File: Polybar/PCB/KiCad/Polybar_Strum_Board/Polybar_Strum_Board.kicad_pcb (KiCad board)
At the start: 2 copper layers, 185 x 38 mm, 25 parts, among them SW1 MX_SW_solder, SW2 MX_SW_solder, SW3 MX_SW_solder, SW4 MX_SW_HS, SW5 MX_SW_HS, U1 ProMicro, U2 RKJXV1224005

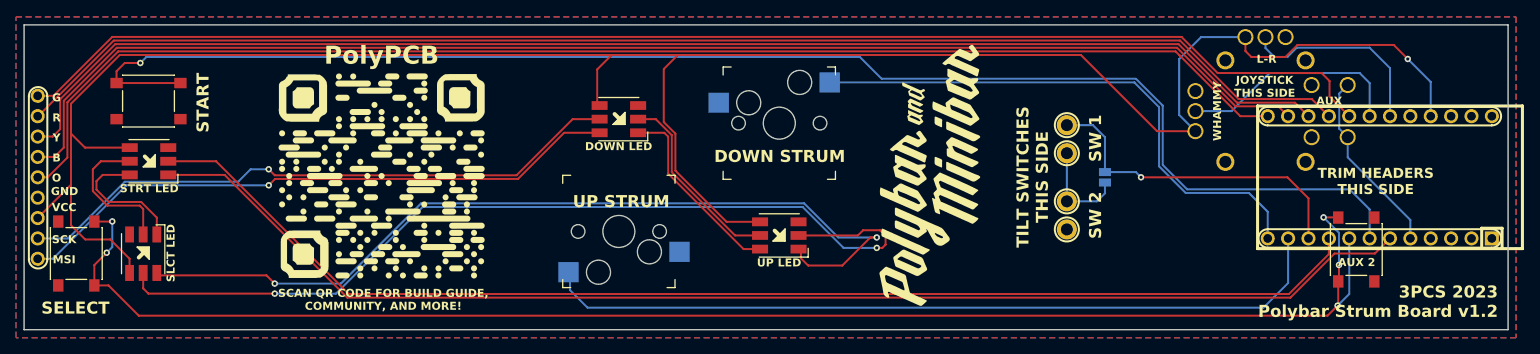
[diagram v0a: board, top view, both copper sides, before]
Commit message: Switched connectors from test pins to an actual connector
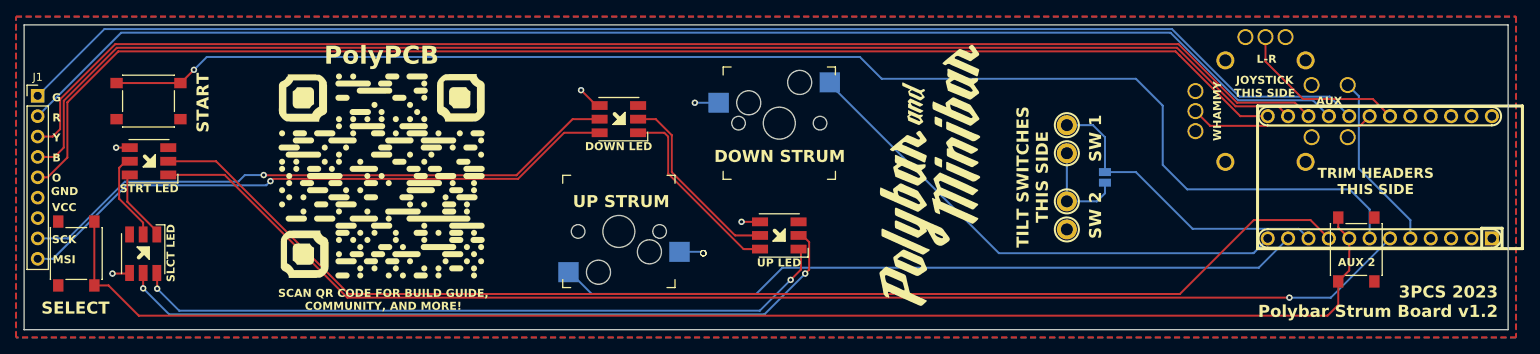
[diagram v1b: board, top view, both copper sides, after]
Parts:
- removed TP10, TP11, TP12, TP14, TP15, TP16, TP4, TP6, TP8: TestPoint, Polybar:test_point
- added J1: Conn_01x09_Pin, Connector_PinHeader_2.54mm:PinHeader_1x09_P2.54mm_Vertical, F.Cu at (23.7, 104.8)
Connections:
- SW1 pad 1: Select -> GND
- SW1 pad 2: GND -> Select
- SW3 pad 1: GND -> Start
- SW3 pad 2: Start -> GND
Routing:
- net VCC: track 273.4 -> 9.26 mm, vias 1 -> 4
- net 2_mosi: track 108.5 -> 87.7 mm
- net 2_sck: track 113.4 -> 93.1 mm
- net Select: track 190.9 -> 177.2 mm, vias 5 -> 0
- net Start: track 182.2 -> 173.4 mm
- net 3_mosi: track 16.0 -> 8.65 mm
- net 3_sck: track 17.5 -> 10.6 mm
- net GND: track 0.00 -> 6.01 mm, vias 0 -> 5
- net Up: track 99.5 -> 93.5 mm
- net VRY: track 28.3 -> 23.0 mm
- net Down: track 69.1 -> 64.4 mm
- net VRX: track 24.9 -> 21.4 mm
- net Tilt: track 41.4 -> 38.5 mm, vias 1 -> 0
- net SW: track 23.2 -> 22.4 mm
- net Red: track 168.8 -> 169.6 mm
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- added copper zone on B.Cu, net VCC
- added copper zone on F.Cu, net VCC
- removed copper zone on B.Cu, net GND

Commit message: re-routed pcb
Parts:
- removed TP1, TP17, TP2, TP3: TestPoint, Polybar:test_point_2
- added SJ2: Conn_01x02_Pin, Connector_PinHeader_2.54mm:PinHeader_1x02_P2.54mm_Vertical, F.Cu at (152.0, 119.4)
- added SJ3: Conn_01x02_Pin, Connector_PinHeader_2.54mm:PinHeader_1x02_P2.54mm_Vertical, F.Cu at (152.0, 109.2)
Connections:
- D1 pad 5: fret_sck -> 2_sck
- D1 pad 6: fret_mosi -> 2_mosi
- D2 pad 1: 2_mosi -> led_mosi
- D2 pad 2: 2_sck -> led_sck
- D3 pad 5: 2_sck -> fret_mosi
- D3 pad 6: 2_mosi -> fret_sck
- D4 pad 1: led_mosi -> 2_mosi
- D4 pad 2: led_sck -> 2_sck
- U2 pad SH: (no net) -> unconnected-(U2-PadSH)
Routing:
- net led_sck: track 156.0 -> 67.3 mm
- net led_mosi: track 161.4 -> 76.8 mm
- net fret_mosi: track 76.3 -> 16.3 mm
- net fret_sck: track 75.9 -> 19.2 mm
- net 2_sck: track 93.1 -> 55.9 mm, vias 2 -> 0
- net 2_mosi: track 87.7 -> 55.9 mm, vias 2 -> 0
- net unconnected-(U2-PadSH): track 0.00 -> 20.0 mm
- net Start: track 173.4 -> 166.0 mm
- net Tilt: track 38.5 -> 35.9 mm
- net Tilt_2: track 12.5 -> 10.3 mm
- net Red: track 169.6 -> 167.9 mm
- net Green: track 171.4 -> 169.7 mm
- net Down: track 64.4 -> 62.9 mm
- net 3_sck: track 10.6 -> 12.1 mm
- net VCC: track 9.26 -> 8.10 mm
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
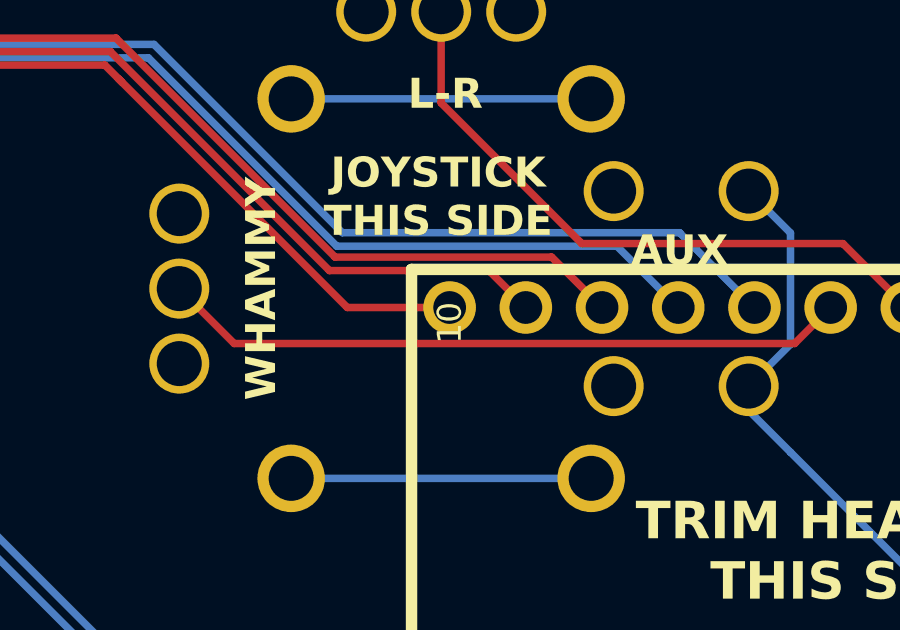
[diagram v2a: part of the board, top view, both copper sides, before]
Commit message: Deleted extra footprints and updated Schematic
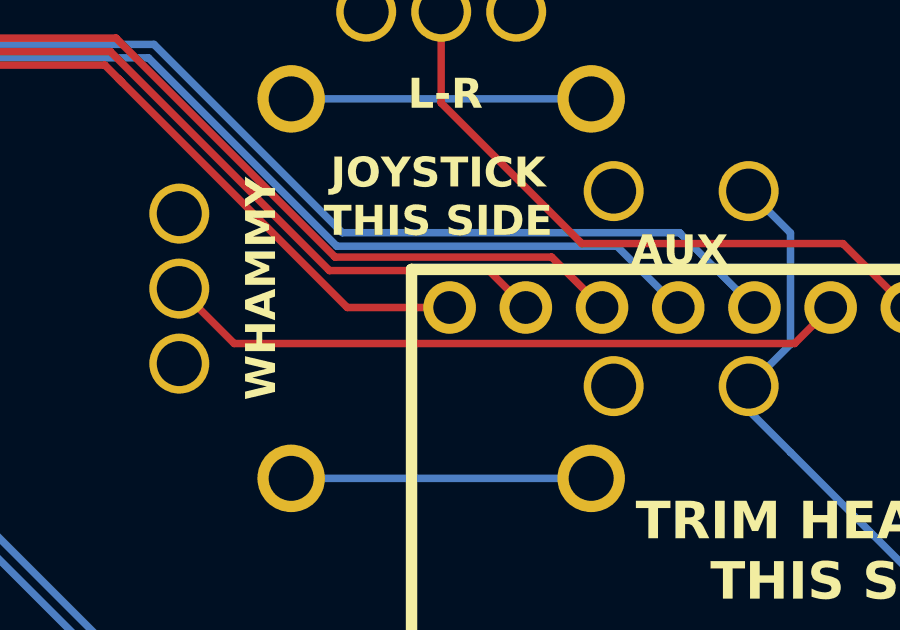
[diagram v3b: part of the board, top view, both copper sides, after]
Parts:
- SJ1: footprint Polybar:Solder_Jumper -> Minibar:Solder_Jumper
- SW4, SW5: footprint Polybar:Kailh_Hotswap_MX -> Minibar:Kailh_Hotswap_MX
- U1: value ProMicro -> KB2040; footprint Polybar:KB2040-ProMicroPins -> Minibar:KB2040
- U2: value RKJXV1224005 -> Joystick; footprint Polybar:RKJXV1224005 -> Minibar:Joystick
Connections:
- U2 pad SH: unconnected-(U2-PadSH) -> SH
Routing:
- net unconnected-(U2-PadSH): track 20.0 -> 0.00 mm
- net SH: track 0.00 -> 20.0 mm
